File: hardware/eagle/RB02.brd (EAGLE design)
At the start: 50 x 50 mm, 20 parts, among them J1 CON_TERMINAL_BLOCK_02-5MM, J2 CON_TERMINAL_BLOCK_02-5MM, J3 CON_TERMINAL_BLOCK_02-5MM, J4 CON_TERMINAL_BLOCK_02-5MM, K1 JS-M1A-12V-5, K2 JS-M1A-12V-5, Q1 BC547, Q2 BC547

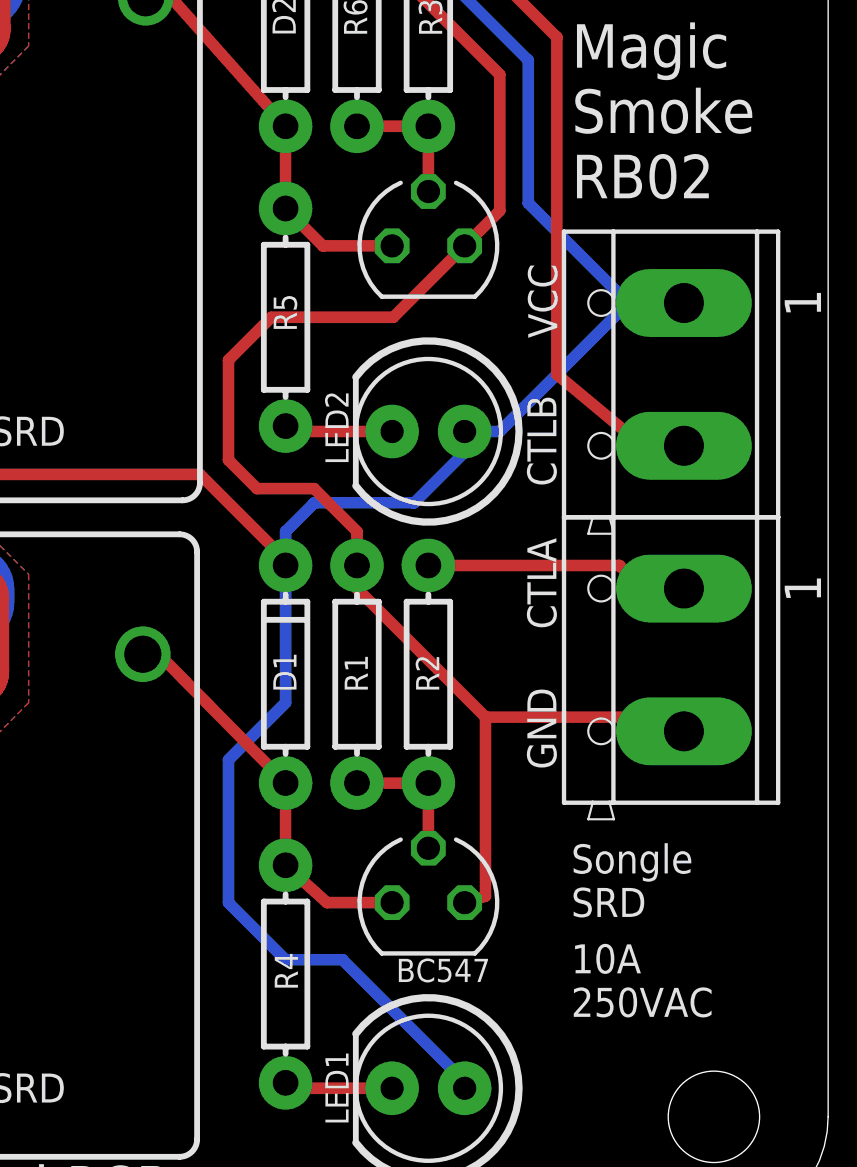
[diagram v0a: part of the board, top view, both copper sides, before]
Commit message: BC337s instead of BC546s
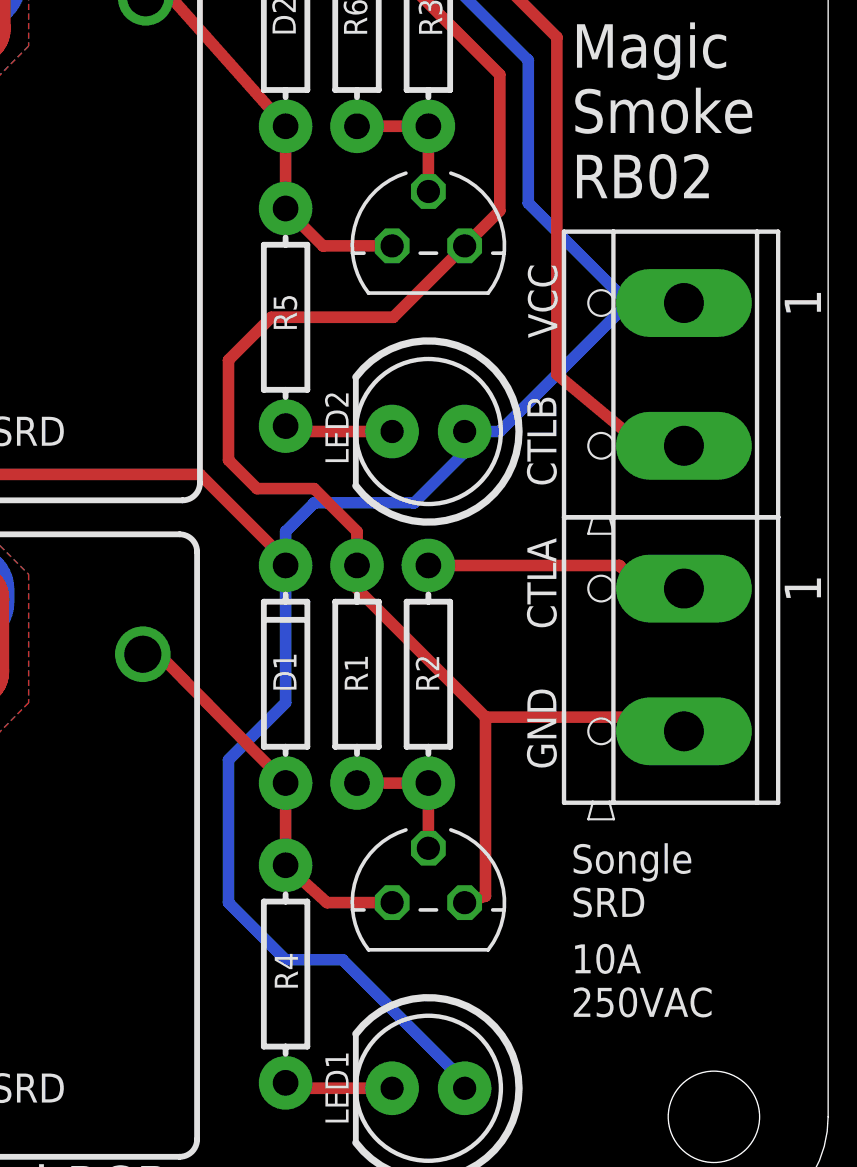
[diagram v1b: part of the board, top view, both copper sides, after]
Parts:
- Q1, Q2: value BC547 -> BC337; device transistor-small-signal:SOT54A -> transistor:TO92
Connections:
- net COIL_A: now also Q1.3; no longer Q1.C
- net COIL_B: now also Q2.3; no longer Q2.C
- net GND: now also Q1.1, Q2.1; no longer Q1.E, Q2.E
- net N$1: now also Q2.2; no longer Q2.B
- net N$6: now also Q1.2; no longer Q1.B
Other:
- board text removed: "BC547"
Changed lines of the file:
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@@
 <text x="3.643" y="25.358" size="1.016" layer="21" ratio="15">Normally</text>
 <text x="40.483" y="21.073" size="1.016" layer="21" ratio="15" rot="R90">CTLA</text>
-<text x="38.173" y="9.533" size="0.8128" layer="21" font="vector" ratio="15" rot="R180">BC547</text>
 <text x="16" y="4.5" size="1.016" layer="21" font="vector" ratio="15">Songle SRD</text>
 <rectangle x1="12.4681" y1="10.5349" x2="18.0307" y2="10.5603" layer="22"/>
@@
 </element>
 <element name="J2" library="dp_devices" package="TERMINAL_BLOCK_2P_5" value="CON_TERMINAL_BLOCK_02-5MM" x="6.5" y="13.5" smashed="yes" rot="R270"/>
-<element name="Q1" library="transistor-small-signal" package="SOT54A" value="BC547" x="36" y="11.5" smashed="yes"/>
+<element name="Q1" library="transistor" package="TO92" value="BC337" x="36" y="11.5" smashed="yes">
+<attribute name="VALUE" x="38" y="9.5" size="0.8128" layer="27" font="vector" ratio="10" rot="R180"/>
+</element>
 <element name="K1" library="relay" package="JS-M1A" value="JS-M1A-12V-5" x="20" y="13.5" smashed="yes" rot="R90">
 <attribute name="OC_NEWARK" value="13P4555" x="20" y="13.5" size="1.778" layer="27" rot="R90" display="off"/>
@@
 </element>
 <element name="J4" library="dp_devices" package="TERMINAL_BLOCK_2P_5" value="CON_TERMINAL_BLOCK_02-5MM" x="6.75" y="36.52" smashed="yes" rot="R270"/>
-<element name="Q2" library="transistor-small-signal" package="SOT54A" value="BC547" x="36" y="34.5" smashed="yes">
-<attribute name="VALUE" x="38.056" y="32.468" size="0.8128" layer="27" font="vector" ratio="10" rot="R180"/>
+<element name="Q2" library="transistor" package="TO92" value="BC337" x="36" y="34.5" smashed="yes">
+<attribute name="VALUE" x="38" y="32.5" size="0.8128" layer="27" font="vector" ratio="10" rot="R180"/>
 </element>
 <element name="K2" library="relay" package="JS-M1A" value="JS-M1A-12V-5" x="20.1" y="36.49" smashed="yes" rot="R90">
@@
 <signal name="GND">
 <contactref element="R1" pad="P$2"/>
-<contactref element="Q1" pad="E"/>
+<contactref element="Q1" pad="1"/>
 <contactref element="R6" pad="P$2"/>
-<contactref element="Q2" pad="E"/>
+<contactref element="Q2" pad="1"/>
 <wire x1="33.5" y1="46.31" x2="33.5" y2="45.5" width="0.4064" layer="1"/>
 <wire x1="33.5" y1="45.5" x2="38.5" y2="40.5" width="0.4064" layer="1"/>
@@
 <contactref element="R2" pad="P$1"/>
 <contactref element="R1" pad="P$1"/>
-<contactref element="Q1" pad="B"/>
+<contactref element="Q1" pad="2"/>
 <wire x1="33.5" y1="15.69" x2="36" y2="15.69" width="0.4064" layer="1"/>
 <wire x1="36" y1="15.69" x2="36" y2="13.405" width="0.4064" layer="1"/>
@@
 <contactref element="D2" pad="A"/>
 <contactref element="R5" pad="P$1"/>
-<contactref element="Q2" pad="C"/>
+<contactref element="Q2" pad="3"/>
 <contactref element="K2" pad="2"/>
 <wire x1="34.73" y1="34.5" x2="32.31" y2="34.5" width="0.4064" layer="1"/>
@@
 <contactref element="R3" pad="P$1"/>
 <contactref element="R6" pad="P$1"/>
-<contactref element="Q2" pad="B"/>
+<contactref element="Q2" pad="2"/>
 <wire x1="33.5" y1="38.69" x2="36" y2="38.69" width="0.4064" layer="1"/>
 <wire x1="36" y1="38.69" x2="36" y2="36.405" width="0.4064" layer="1"/>
@@
 <contactref element="D1" pad="A"/>
 <contactref element="R4" pad="P$1"/>
-<contactref element="Q1" pad="C"/>
+<contactref element="Q1" pad="3"/>
 <contactref element="K1" pad="2"/>
 <wire x1="31" y1="12.81" x2="31" y2="15.69" width="0.4064" layer="1"/>
